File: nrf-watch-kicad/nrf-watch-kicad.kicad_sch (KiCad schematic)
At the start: 91 parts, among them IC1 TLV840MAPL36DBVRQ1, IC2 XC9265C181MR-G, IC3 TPS61023DRLT, IC4 MAX30101EFD+T, M1 Vibrator DC Motor, Q1 DMP2045U-7, Q2 SS8050-G, U1 MAX1811ESA+, U2 DMC2400UV-7, U3 LIS2DS12TR, U4 MX25R6435FZNIL0, U5 u-blox ANNA-B402, U6 DRV2603RUNT, U7 XC9265A331MR-G, U8 TXB0104QRUTRQ1, U9 GC9A01

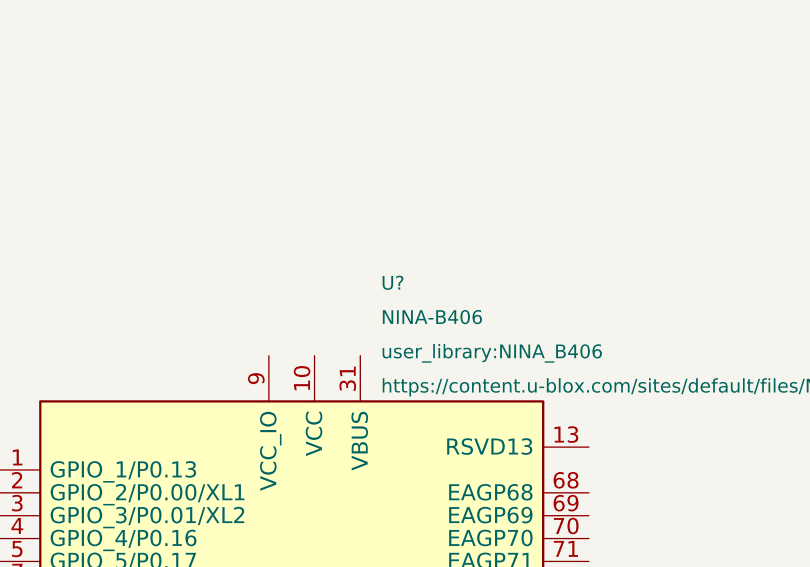
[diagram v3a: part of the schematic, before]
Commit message: Improved time handling by retaining the clock when reset and syncing over BLE.
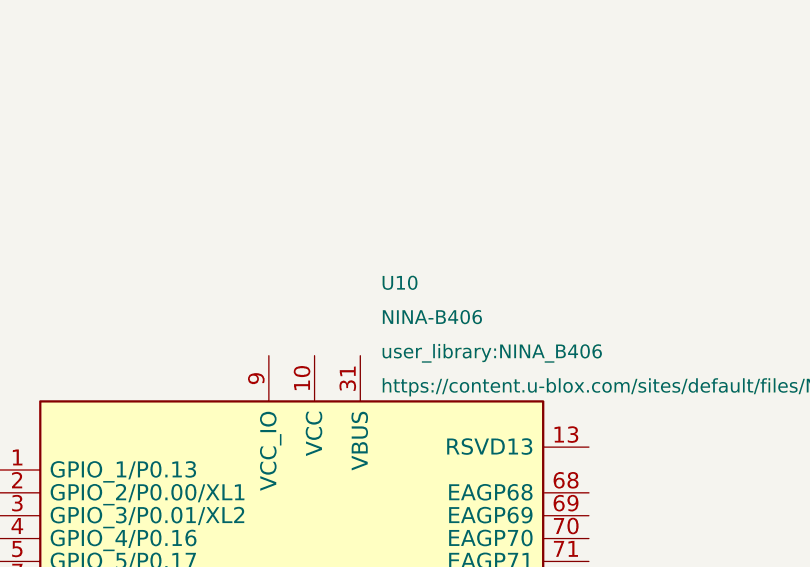
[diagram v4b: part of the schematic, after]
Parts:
- CHG+1: footprint TestPoint:TestPoint_Pad_D1.5mm -> TestPoint:TestPoint_THTPad_D1.0mm_Drill0.5mm
- CHG-1: footprint TestPoint:TestPoint_Pad_1.5x1.5mm -> TestPoint:TestPoint_THTPad_D1.0mm_Drill0.5mm
- TP12, TP2, TP4, TP8: footprint TestPoint:TestPoint_Pad_D1.0mm -> TestPoint:TestPoint_THTPad_D1.0mm_Drill0.5mm
- gave numbers to parts that had none: 1
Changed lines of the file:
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@@
       (effects (font (size 1.27 1.27)) (justify left) hide)
     )
-    (property "Footprint" "TestPoint:TestPoint_Pad_1.5x1.5mm" (id 2) (at 33.02 35.56 0)
+    (property "Footprint" "TestPoint:TestPoint_THTPad_D1.0mm_Drill0.5mm" (id 2) (at 33.02 35.56 0)
       (effects (font (size 1.27 1.27)) hide)
     )
@@
       (effects (font (size 1.27 1.27)) (justify left))
     )
-    (property "Footprint" "TestPoint:TestPoint_Pad_D1.0mm" (id 2) (at 147.32 180.34 0)
+    (property "Footprint" "TestPoint:TestPoint_THTPad_D1.0mm_Drill0.5mm" (id 2) (at 147.32 180.34 0)
       (effects (font (size 1.27 1.27)) hide)
     )
@@
       (effects (font (size 1.27 1.27)) (justify left))
     )
-    (property "Footprint" "TestPoint:TestPoint_Pad_D1.0mm" (id 2) (at 139.7 180.34 0)
+    (property "Footprint" "TestPoint:TestPoint_THTPad_D1.0mm_Drill0.5mm" (id 2) (at 139.7 180.34 0)
       (effects (font (size 1.27 1.27)) hide)
     )
@@
       (effects (font (size 1.27 1.27)) (justify left))
     )
-    (property "Footprint" "TestPoint:TestPoint_Pad_D1.0mm" (id 2) (at 266.7 43.18 0)
+    (property "Footprint" "TestPoint:TestPoint_THTPad_D1.0mm_Drill0.5mm" (id 2) (at 266.7 43.18 0)
       (effects (font (size 1.27 1.27)) hide)
     )
@@
       (effects (font (size 1.27 1.27)) (justify left))
     )
-    (property "Footprint" "TestPoint:TestPoint_Pad_D1.0mm" (id 2) (at 132.08 180.34 0)
+    (property "Footprint" "TestPoint:TestPoint_THTPad_D1.0mm_Drill0.5mm" (id 2) (at 132.08 180.34 0)
       (effects (font (size 1.27 1.27)) hide)
     )
@@
   (symbol (lib_id "user_library:NINA-B406") (at -153.9421 180.655 0) (unit 1)
     (in_bom yes) (on_board yes) (fields_autoplaced)
-    (property "Reference" "U?" (id 0) (at -116.0833 167.5309 0)
+    (property "Reference" "U10" (id 0) (at -116.0833 167.5309 0)
       (effects (font (size 1.524 1.524)) (justify left))
     )
@@
       (effects (font (size 1.27 1.27)) (justify left) hide)
     )
-    (property "Footprint" "TestPoint:TestPoint_Pad_D1.5mm" (id 2) (at 30.48 35.56 0)
+    (property "Footprint" "TestPoint:TestPoint_THTPad_D1.0mm_Drill0.5mm" (id 2) (at 30.48 35.56 0)
       (effects (font (size 1.27 1.27)) hide)
     )
@@
     )
     (path "/de456328-f504-4677-938f-38bfdca72aa8"
-      (reference "CHG+1") (unit 1) (value "Conn_01x01_Male") (footprint "TestPoint:TestPoint_Pad_D1.5mm")
+      (reference "CHG+1") (unit 1) (value "Conn_01x01_Male") (footprint "TestPoint:TestPoint_THTPad_D1.0mm_Drill0.5mm")
     )
     (path "/108f71b5-6a25-47e4-8610-963b7bfe276c"
-      (reference "CHG-1") (unit 1) (value "Conn_01x01_Male") (footprint "TestPoint:TestPoint_Pad_1.5x1.5mm")
+      (reference "CHG-1") (unit 1) (value "Conn_01x01_Male") (footprint "TestPoint:TestPoint_THTPad_D1.0mm_Drill0.5mm")
     )
     (path "/d11282ce-8047-4886-8af8-708426f64b4b"
@@
     )
     (path "/687ce67f-1f86-4d71-82bb-8f0aec146ef8"
-      (reference "TP2") (unit 1) (value "MR") (footprint "TestPoint:TestPoint_Pad_D1.0mm")
+      (reference "TP2") (unit 1) (value "MR") (footprint "TestPoint:TestPoint_THTPad_D1.0mm_Drill0.5mm")
     )
     (path "/f6304d4c-731d-49c2-a494-dc5b8b3a7156"
@@
     )
     (path "/1b717e34-7b2a-413d-beb9-dece96db388a"
-      (reference "TP4") (unit 1) (value "MR") (footprint "TestPoint:TestPoint_Pad_D1.0mm")
+      (reference "TP4") (unit 1) (value "MR") (footprint "TestPoint:TestPoint_THTPad_D1.0mm_Drill0.5mm")
     )
     (path "/0d429f8b-e614-4807-b8b7-ade9fbecccf8"
@@
     )
     (path "/7d3d73ab-e60f-4595-b58d-3a77b4c7c767"
-      (reference "TP8") (unit 1) (value "1V8") (footprint "TestPoint:TestPoint_Pad_D1.0mm")
+      (reference "TP8") (unit 1) (value "1V8") (footprint "TestPoint:TestPoint_THTPad_D1.0mm_Drill0.5mm")
     )
     (path "/0fe871c1-4641-46c3-a67b-3235850e9592"
@@
     )
     (path "/a72e2a2f-0ae6-4e4a-b949-4618826dfa2b"
-      (reference "TP12") (unit 1) (value "MR") (footprint "TestPoint:TestPoint_Pad_D1.0mm")
+      (reference "TP12") (unit 1) (value "MR") (footprint "TestPoint:TestPoint_THTPad_D1.0mm_Drill0.5mm")
     )
     (path "/ac0310d6-e2c2-402b-85e7-52ac9f2a21a1"
@@
     )
     (path "/bc223fa1-6d6e-482b-8f2d-79b246ea5c7d"
-      (reference "U?") (unit 1) (value "NINA-B406") (footprint "user_library:NINA_B406")
-    )
-  )
+      (reference "U10") (unit 1) (value "NINA-B406") (footprint "user_library:NINA_B406")
+    )
+  )

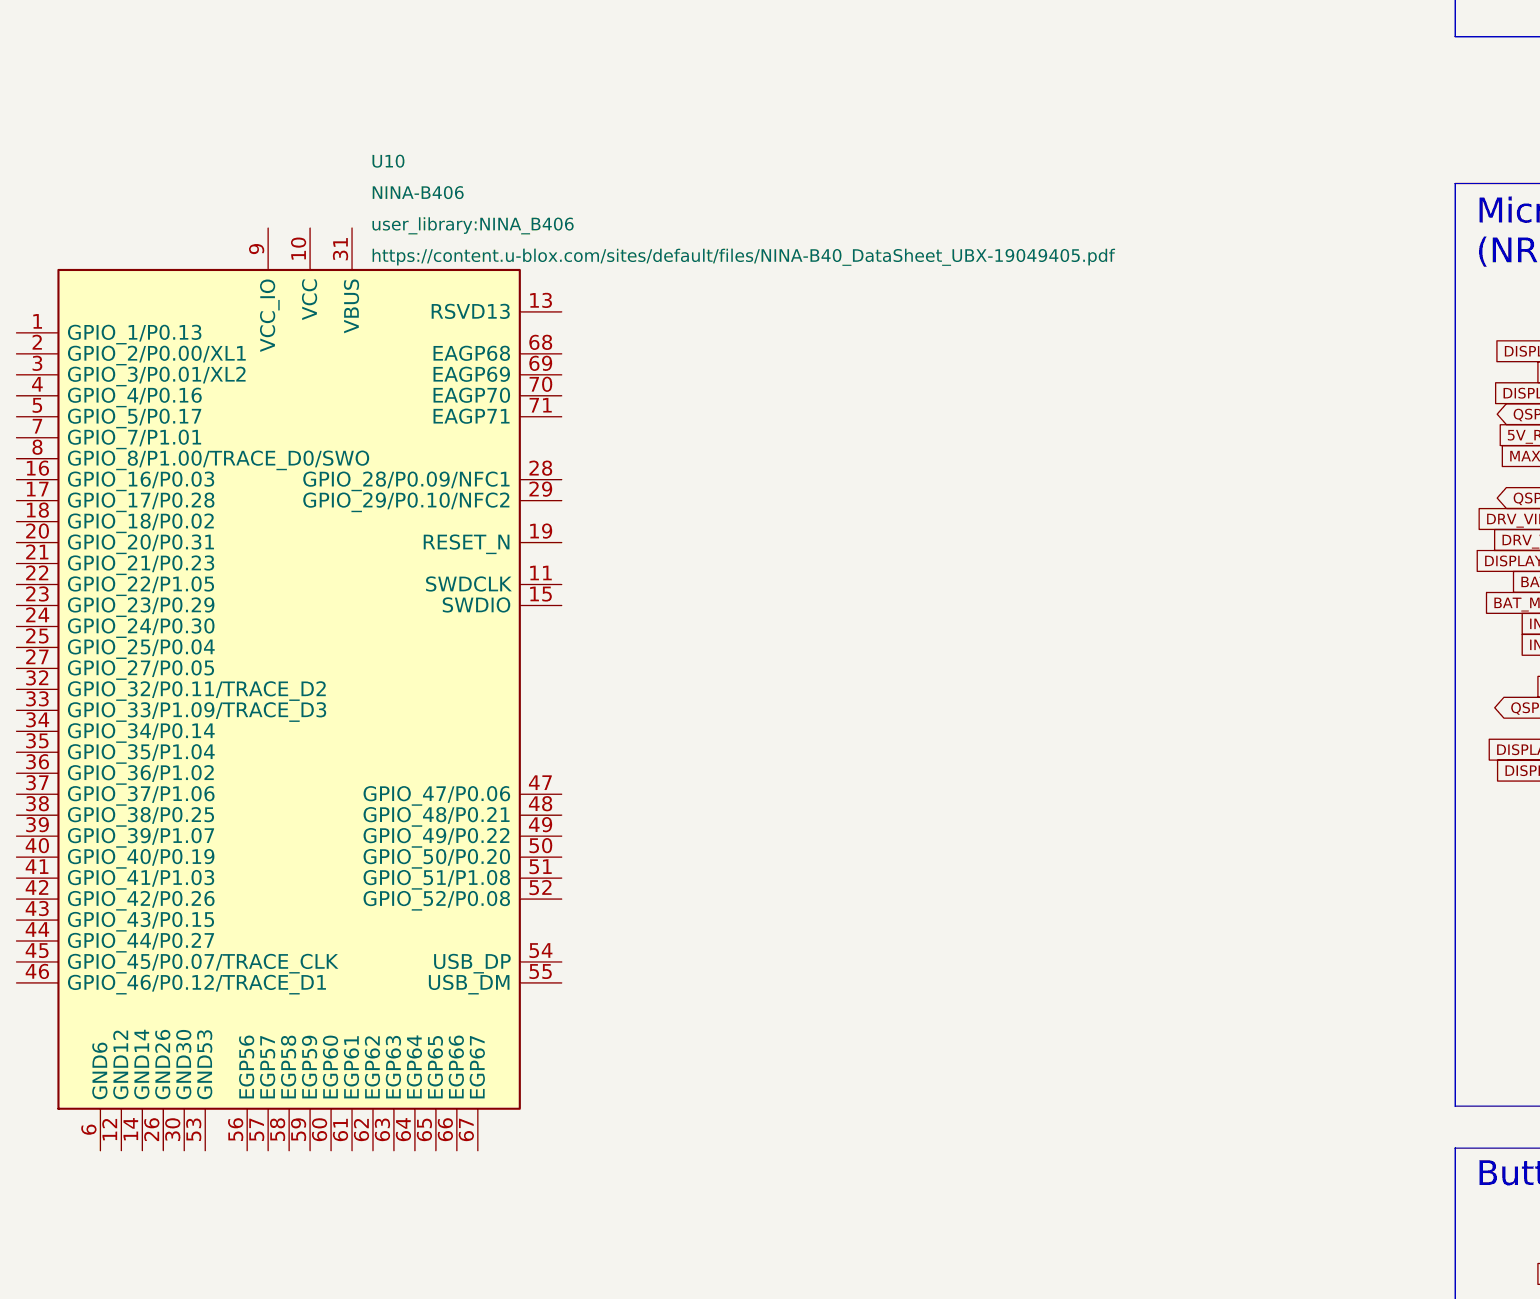
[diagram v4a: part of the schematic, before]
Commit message: Add exported schematic of the watch.
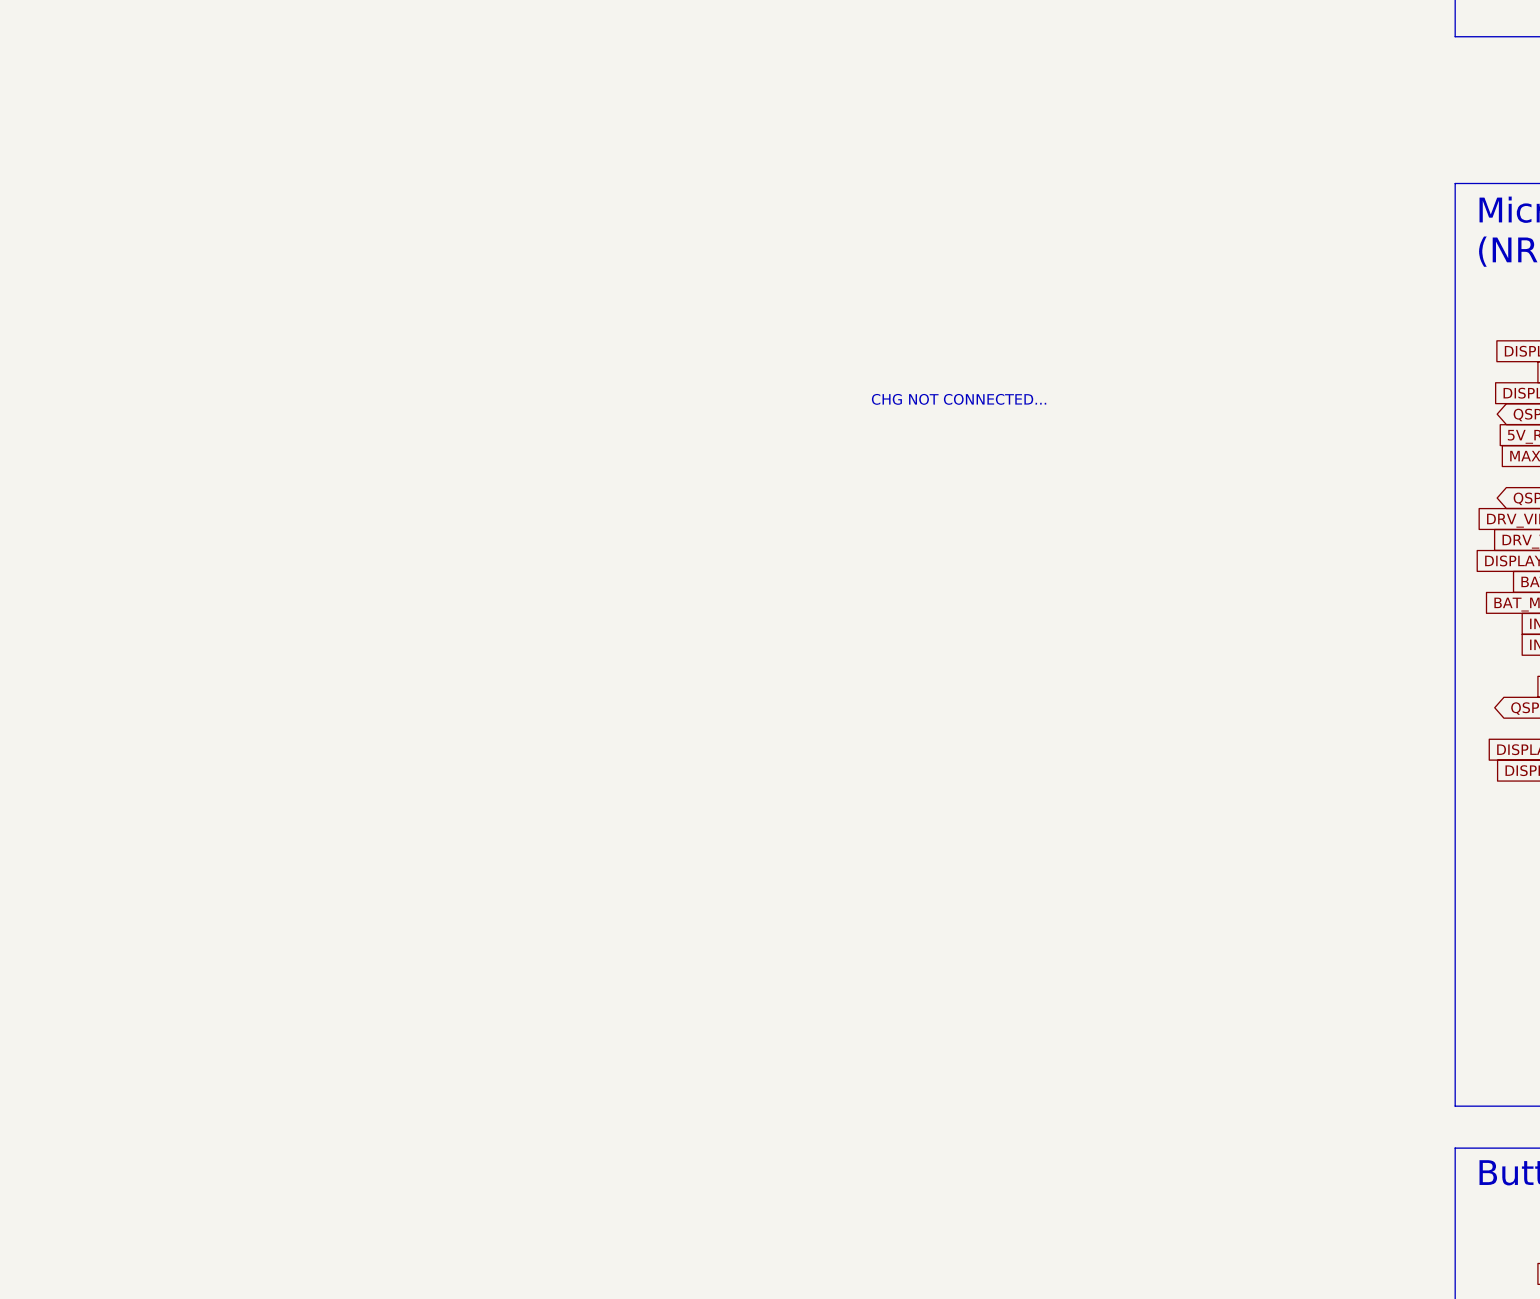
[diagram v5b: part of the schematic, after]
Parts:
- removed U10: NINA-B406, user_library:NINA_B406, symbol user_library:NINA-B406
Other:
- note added: "CHG NOT CONNECTED..."
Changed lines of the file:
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@@
     (effects (font (size 1.27 1.27)) (justify left bottom))
   )
+  (text "CHG NOT CONNECTED..." (at -55.5092 197.3675 0)
+    (effects (font (size 1.27 1.27)) (justify left bottom))
+  )
   (text "Buttons" (at 17.78 292.1 0)
     (effects (font (size 3 3)) (justify left bottom))
@@
     (pin "2")
   )
-  (symbol (lib_id "user_library:NINA-B406") (at -153.9421 180.655 0) (unit 1)
-    (in_bom yes) (on_board yes) (fields_autoplaced)
-    (property "Reference" "U10" (id 0) (at -116.0833 167.5309 0)
-      (effects (font (size 1.524 1.524)) (justify left))
-    )
-    (property "Value" "NINA-B406" (id 1) (at -116.0833 171.3409 0)
-      (effects (font (size 1.524 1.524)) (justify left))
-    )
-    (property "Footprint" "user_library:NINA_B406" (id 2) (at -116.0833 175.1509 0)
-      (effects (font (size 1.524 1.524)) (justify left))
-    )
-    (property "Datasheet" "https://content.u-blox.com/sites/default/files/NINA-B40_DataSheet_UBX-19049405.pdf" (id 3) (at -116.0833 178.9609 0)
-      (effects (font (size 1.524 1.524)) (justify left))
-    )
-    (pin "1")
-    (pin "10")
-    (pin "11")
-    (pin "12")
-    (pin "13")
-    (pin "14")
-    (pin "15")
-    (pin "16")
-    (pin "17")
-    (pin "18")
-    (pin "19")
-    (pin "2")
-    (pin "20")
-    (pin "21")
-    (pin "22")
-    (pin "23")
-    (pin "24")
-    (pin "25")
-    (pin "26")
-    (pin "27")
-    (pin "28")
-    (pin "29")
-    (pin "3")
-    (pin "30")
-    (pin "31")
-    (pin "32")
-    (pin "33")
-    (pin "34")
-    (pin "35")
-    (pin "36")
-    (pin "37")
-    (pin "38")
-    (pin "39")
-    (pin "4")
-    (pin "40")
-    (pin "41")
-    (pin "42")
-    (pin "43")
-    (pin "44")
-    (pin "45")
-    (pin "46")
-    (pin "47")
-    (pin "48")
-    (pin "49")
-    (pin "5")
-    (pin "50")
-    (pin "51")
-    (pin "52")
-    (pin "53")
-    (pin "54")
-    (pin "55")
-    (pin "56")
-    (pin "57")
-    (pin "58")
-    (pin "59")
-    (pin "6")
-    (pin "60")
-    (pin "61")
-    (pin "62")
-    (pin "63")
-    (pin "64")
-    (pin "65")
-    (pin "66")
-    (pin "67")
-    (pin "68")
-    (pin "69")
-    (pin "7")
-    (pin "70")
-    (pin "71")
-    (pin "8")
-    (pin "9")
-  )
   (symbol (lib_id "power:GND") (at 43.18 40.64 0) (unit 1)
     (in_bom yes) (on_board yes)
@@
       (reference "U9") (unit 1) (value "GC9A01") (footprint "user_library:GC9A01_disp")
     )
-    (path "/bc223fa1-6d6e-482b-8f2d-79b246ea5c7d"
-      (reference "U10") (unit 1) (value "NINA-B406") (footprint "user_library:NINA_B406")
-    )
   )
